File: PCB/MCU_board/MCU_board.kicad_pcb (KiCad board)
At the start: 2 copper layers, 70 x 70 mm, 45 parts, among them IC1 NEO-F10N-00B, IC2 TXB0104PWR, IC3 ESP32-S3-WROOM-1-N4R8, IC6 4259-63, IC8 MAX98357AETE+T, J13 Conn_01x15, J14 Conn_01x15, J2 Speaker, J4 FXP612 (u.FL) 2, J5 FXP612 (u.FL) 1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

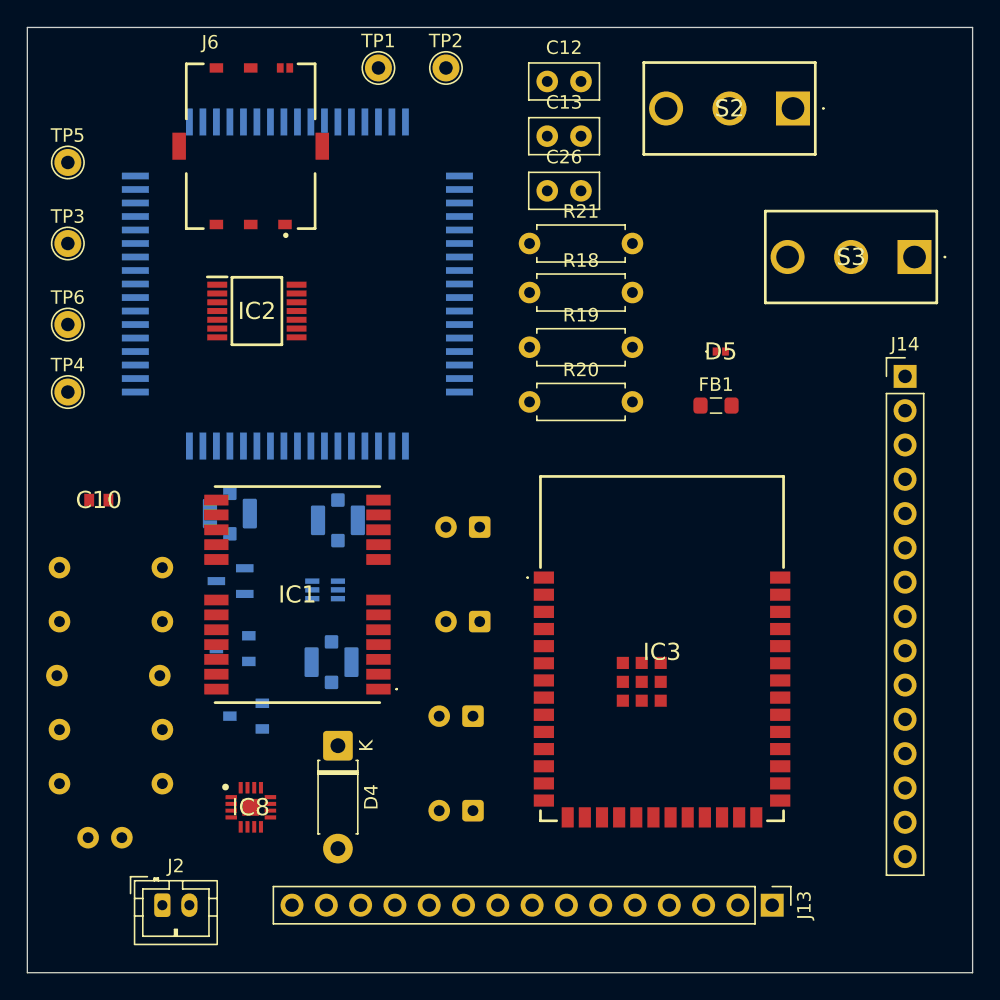
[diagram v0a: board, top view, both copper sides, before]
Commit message: routing and holes added
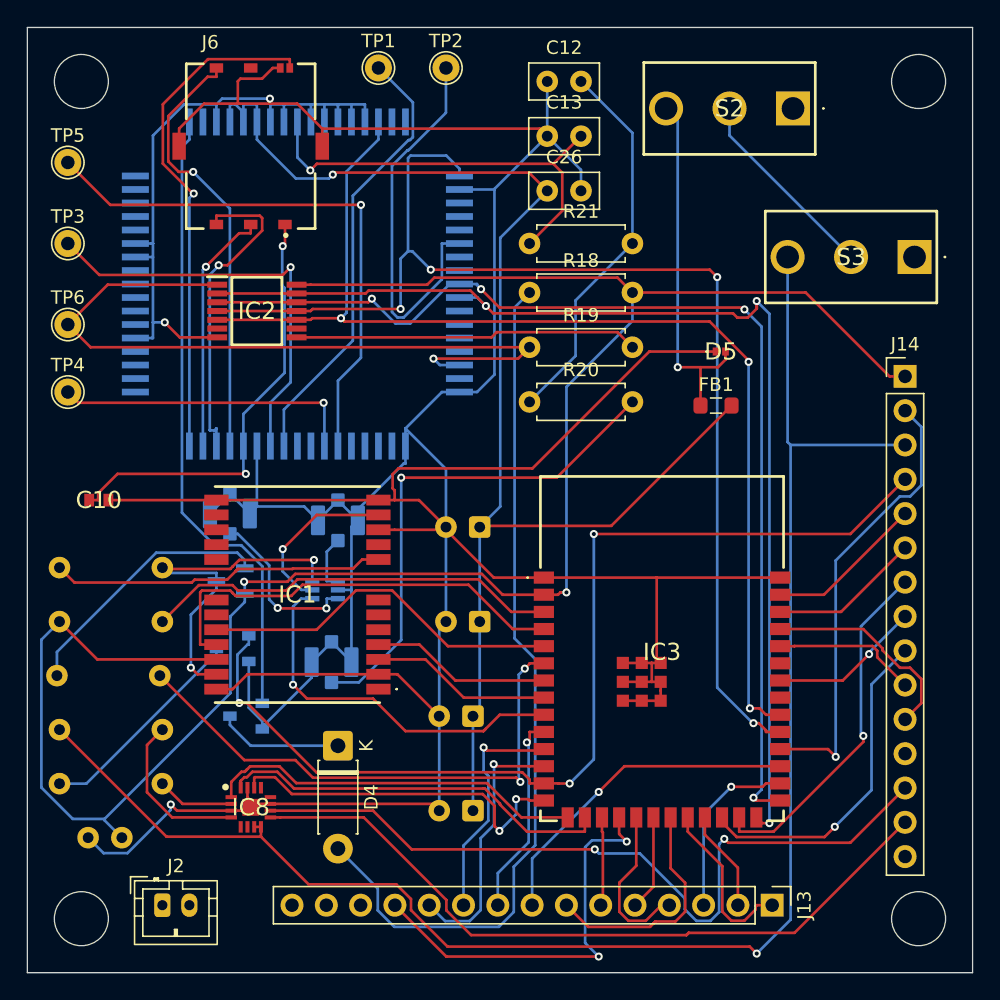
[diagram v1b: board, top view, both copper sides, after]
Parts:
- TP1: value TestPoint -> USB_DP
- TP2: value TestPoint -> BOOT_CFG
- TP3: value TestPoint -> USB_DM
- TP4: value TestPoint -> USB_VBUS
- TP5: value TestPoint -> MDM_LOG_TX
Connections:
- IC8 pad 10: Net-(IC8-OUTN) -> /OUT_N
- IC8 pad 9: Net-(IC8-OUTP) -> /OUT_P
- J14 pad 13: unconnected-(J14-Pin_13-Pad13) -> /OUT_N
- J14 pad 14: unconnected-(J14-Pin_14-Pad14) -> /OUT_P
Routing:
- net GND: track 0.00 -> 365.5 mm, vias 0 -> 3
- net /+3V3: track 0.00 -> 152.4 mm, vias 0 -> 2
- net /OUT+5V: track 0.00 -> 121.4 mm, vias 0 -> 1
- net Net-(U2-VBAT@1): track 0.00 -> 101.5 mm, vias 0 -> 1
- net /PWRKEY: track 0.00 -> 90.4 mm, vias 0 -> 4
- net /GSM_RXT: track 0.00 -> 86.4 mm, vias 0 -> 3
- net /STATUS: track 0.00 -> 85.0 mm, vias 0 -> 3
- net /GSM_TXD: track 0.00 -> 81.9 mm, vias 0 -> 4
- net /LOUDNESS: track 0.00 -> 76.5 mm, vias 0 -> 3
- net Net-(D4-A): track 0.00 -> 64.5 mm
- net /OUT_N: track 0.00 -> 58.1 mm, vias 0 -> 2
- net /Stationary/GSM_sheet/OUT1.8V: track 0.00 -> 56.8 mm, vias 0 -> 1
- net /OUT_P: track 0.00 -> 54.8 mm
- net Net-(Q5-G): track 0.00 -> 46.9 mm
- net Net-(U2-MDM_LOG_TX): track 0.00 -> 41.6 mm, vias 0 -> 1
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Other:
- outline, holes or cut-outs redrawn
- board text added: "Conn_01x15"

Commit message: everything before jlc template
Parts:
- removed J13, J14: Conn_01x15, Connector_PinHeader_2.54mm:PinHeader_1x15_P2.54mm_Vertical
- removed J2: Speaker, Connector_JST:JST_PH_B2B-PH-K_1x02_P2.00mm_Vertical
- added C1: 100nF, Capacitor_THT:C_Disc_D5.0mm_W2.5mm_P2.50mm, F.Cu at (219.5, 84.0)
- added C2: 1μF, Capacitor_THT:C_Disc_D5.0mm_W2.5mm_P2.50mm, F.Cu at (211.0, 94.0)
- added C3: 100nF, Capacitor_THT:C_Disc_D5.0mm_W2.5mm_P2.50mm, F.Cu at (211.0, 98.1)
- added J1: DS1013-40SSIB1-B-0, DS1013-40SSIB1-B-0:DS101340SSIB1B0, F.Cu at (236.0, 93.3)
- added R30: 10kΩ, Resistor_THT:R_Axial_DIN0207_L6.3mm_D2.5mm_P7.62mm_Horizontal, F.Cu at (255.0, 98.8)
- added S1: 1825910-6, 1825910-6:18259106, F.Cu at (219.5, 93.0)
- added S4: 1825910-6, 1825910-6:18259106, F.Cu at (242.5, 93.0)
- C22: value 100nF -> 1000nF
- moved R18 24.0 mm to (254.2, 42.6)
- moved R19 24.0 mm to (254.2, 46.7)
- moved R20 24.0 mm to (254.2, 50.7)
- moved R21 24.0 mm to (254.2, 39.0)
- moved D5 12.6 mm to (249.3, 42.0)
- moved FB1 12.6 mm to (249.0, 46.0)
- moved IC3 11.8 mm to (252.8, 75.3)
- moved C13 10.8 mm to (242.5, 42.0)
- moved C26 10.8 mm to (242.5, 46.0)
- moved S3 10.0 mm to (259.4, 57.0)
- moved IC8 3.62 mm to (207.8, 85.5)
- moved D4 3.01 mm to (214.0, 83.0)
- moved S2 2.02 mm to (250.4, 34.0)
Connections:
- IC3 pad 13: /LOUDNESS -> /USB_D-
- IC3 pad 14: /G_LRCLK -> /USB_D+
- IC3 pad 26: /GSM_RXT -> unconnected-(IC3-IO45-Pad26)
- IC3 pad 27: /GSM_TXD -> Net-(IC3-IO0)
- IC3 pad 33: unconnected-(IC3-IO40-Pad33) -> /GSM_RXT
- IC3 pad 34: /STAT2 -> /GSM_TXD
- IC3 pad 35: unconnected-(IC3-IO42-Pad35) -> /STAT2
- IC3 pad 38: /USB_D- -> /LOUDNESS
- IC3 pad 39: /USB_D+ -> /G_LRCLK
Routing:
- net /+3V3: track 152.4 -> 224.6 mm
- net GND: track 365.5 -> 437.6 mm, vias 3 -> 7
- net /G_LRCLK: track 26.4 -> 90.5 mm, vias 2 -> 6
- net /ACCEL_CS: track 12.6 -> 64.7 mm, vias 0 -> 1
- net /DATA_IN: track 7.07 -> 58.1 mm, vias 0 -> 3
- net Net-(IC3-EN): track 30.9 -> 77.1 mm, vias 0 -> 4
- net /STATUS: track 85.0 -> 130.3 mm, vias 3 -> 5
- net /STAT2: track 11.3 -> 48.9 mm, vias 1 -> 2
- net /ANTENA_SW: track 28.2 -> 64.1 mm
- net /ACCEL_INT1: track 7.51 -> 43.3 mm, vias 0 -> 2
- net /OUT+5V: track 121.4 -> 87.5 mm, vias 1 -> 0
- net /IMU_CS: track 6.59 -> 36.4 mm, vias 0 -> 1
- net Net-(IC3-IO0): track 0.00 -> 27.9 mm
- net /ACCEL_INT2: track 13.3 -> 40.2 mm, vias 1 -> 4
- net /Stationary/GSM_sheet/OUT1.8V: track 56.8 -> 83.3 mm, vias 1 -> 2
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
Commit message: routing on your own
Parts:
- removed C2: 1μF, Capacitor_THT:C_Disc_D5.0mm_W2.5mm_P2.50mm
- removed D5: PESD3V3L1BSLZ, PESD3V3L1BSLZ:PESD3V3L1BSLZ
- removed Q4: BSS138, BSS138:SOT95P240X120-3N
- removed S2, S3: SLW-1276864-4A-D, SLW-1276864-4A-D:SLW12768644AD
- added C4: 1μF, Capacitor_THT:CP_Radial_Tantal_D5.0mm_P2.50mm, F.Cu at (119.0, 120.5)
- added D1: PESD5V0C1BSFYL, PESD5V0C1BSFYL:PMEG3005AESFYL, B.Cu at (54.4, 128.0)
- C1: value 100nF -> 1μF
- C10, FB1, IC1, J6: moved to B.Cu
- C22: footprint Capacitor_THT:CP_Radial_Tantal_D5.0mm_P2.50mm -> Capacitor_THT:C_Disc_D5.0mm_W2.5mm_P2.50mm; moved to F.Cu
- C23: value 100µF -> 1000µF; moved to F.Cu
- C24, C25, C8, IC6, J4, J5, J7, Q3, R17, R26, R29, U2: moved to F.Cu
- R16: value 680kΩ -> 100kΩ; moved to F.Cu
- moved R18 237.3 mm to (40.8, 146.5), turned to 180 degrees
- moved R21 228.9 mm to (49.5, 141.5), turned to -90 degrees
- moved R20 224.0 mm to (58.5, 159.7), turned to -90 degrees
- moved C13 214.7 mm to (49.0, 135.0), turned to -90 degrees
- moved FB1 212.5 mm to (52.0, 125.7), turned to -90 degrees
- moved TP1 209.3 mm to (32.9, 126.8), turned to 180 degrees
- moved C12 209.2 mm to (61.4, 154.3), turned to 180 degrees
- moved C26 203.3 mm to (62.0, 139.5), turned to -90 degrees
- moved C25 199.8 mm to (34.2, 140.5)
- moved C24 198.2 mm to (37.8, 140.0), turned to 0 degrees
- moved R19 197.1 mm to (90.2, 156.0)
- moved R28 192.1 mm to (35.5, 162.3), turned to 90 degrees
- moved J6 190.7 mm to (37.0, 117.9), turned to -90 degrees
- moved IC1 188.8 mm to (47.0, 160.0), turned to 180 degrees
- moved C22 186.2 mm to (54.0, 134.5), turned to 0 degrees
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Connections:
- C8 pad 1: /+3V3 -> Net-(IC1-VCC)
- FB1 pad 1: Net-(D5-K2) -> /3V8
- IC1 pad 22: /+3V3 -> Net-(IC1-VCC)
- J1 pad 26: unconnected-(J1-Pad26) -> /3V8
- R16 pad 2: /OUT+5V -> /LOUDNESS
- R26 pad 2: Net-(Q4-D) -> GND
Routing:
- net GND: track 437.6 -> 0.00 mm, vias 7 -> 0
- net /+3V3: track 224.6 -> 0.00 mm, vias 2 -> 0
- net /STATUS: track 130.3 -> 0.00 mm, vias 5 -> 0
- net /PWRKEY: track 104.2 -> 0.00 mm, vias 4 -> 0
- net /G_LRCLK: track 90.5 -> 0.00 mm, vias 6 -> 0
- net /OUT+5V: track 87.5 -> 0.00 mm
- net /GSM_RXT: track 98.1 -> 11.6 mm, vias 3 -> 1
- net /GSM_TXD: track 85.2 -> 0.00 mm, vias 4 -> 0
- net Net-(D4-A): track 85.1 -> 4.48 mm, vias 1 -> 0
- net /Stationary/GSM_sheet/OUT1.8V: track 83.3 -> 11.9 mm, vias 2 -> 0
- net Net-(U2-VBAT@1): track 105.8 -> 35.0 mm
- net /ACCEL_CS: track 64.7 -> 0.00 mm, vias 1 -> 0
- net Net-(IC3-EN): track 77.1 -> 12.6 mm, vias 4 -> 0
- net Net-(J7-In): track 64.1 -> 0.00 mm, vias 1 -> 0
- net /OUT_P: track 59.5 -> 0.00 mm, vias 2 -> 0
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- added copper zone on In1.Cu, net /+3V3
- added copper zone on In2.Cu, net GND
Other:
- copper layers 2 -> 4

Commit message: routing done
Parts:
- moved C4 40.0 mm to (79.0, 120.3)
- moved C3 27.3 mm to (87.7, 120.5), turned to 180 degrees
- moved D1 20.3 mm to (46.1, 109.4)
- moved R30 16.0 mm to (78.2, 166.5), turned to 180 degrees
- moved FB1 13.5 mm to (54.6, 112.5), turned to 0 degrees
- moved C10 11.6 mm to (46.8, 116.3)
- moved C8 5.20 mm to (95.8, 118.8)
- moved Q3 3.91 mm to (97.3, 123.9)
- moved Q5 2.47 mm to (48.5, 123.8)
- moved J7 0.78 mm to (52.2, 156.3)
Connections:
- J1 pad 11: /USB_D- -> unconnected-(J1-Pad11)
- J1 pad 2: /WCLK -> /3V8
- J1 pad 20: /ACCEL_INT2 -> /ACCEL_INT1
- J1 pad 22: /ACCEL_INT1 -> /ACCEL_INT2
- J1 pad 26: /3V8 -> /WCLK
- J1 pad 37: unconnected-(J1-Pad37) -> /USB_D+
- J1 pad 39: unconnected-(J1-Pad39) -> /USB_D-
- J1 pad 6: /MOSI -> /MISO
- J1 pad 8: /MISO -> /MOSI
- J1 pad 9: /USB_D+ -> unconnected-(J1-Pad9)
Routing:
- net /+3V3: track 0.00 -> 179.2 mm, vias 0 -> 2
- net GND: track 0.00 -> 142.0 mm, vias 0 -> 36
- net /Stationary/GSM_sheet/OUT1.8V: track 11.9 -> 123.8 mm, vias 0 -> 2
- net /PWRKEY: track 0.00 -> 99.1 mm, vias 0 -> 5
- net /GSM_TXD: track 0.00 -> 98.2 mm, vias 0 -> 10
- net /STATUS: track 0.00 -> 92.6 mm, vias 0 -> 3
- net /GSM_RXT: track 11.6 -> 97.4 mm, vias 1 -> 7
- net Net-(IC1-VCC): track 49.6 -> 133.3 mm, vias 1 -> 4
- net /GSM_INT: track 0.00 -> 77.4 mm, vias 0 -> 6
- net /TXD: track 0.00 -> 76.4 mm, vias 0 -> 2
- net /RXD: track 0.00 -> 74.9 mm, vias 0 -> 2
- net /TIMEPULSE: track 0.00 -> 73.9 mm, vias 0 -> 6
- net /G_LRCLK: track 0.00 -> 54.8 mm, vias 0 -> 2
- net /OUT+5V: track 0.00 -> 51.7 mm, vias 0 -> 3
- net /TS/CTRL: track 0.00 -> 51.0 mm, vias 0 -> 2
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- added copper zone on In1.Cu, net GND
- removed copper zone on In1.Cu, net /+3V3
- removed copper zone on In2.Cu, net GND

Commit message: DRC passed
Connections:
- IC2 pad 2: /GSM_RXT -> /Stationary/GSM_sheet/GSM_RXD_1V8
- IC2 pad 3: /GSM_TXD -> /Stationary/GSM_sheet/GSM_TXD_1V8
- IC2 pad 4: /PWRKEY -> /Stationary/GSM_sheet/PWRKEY_1V8
- IC2 pad 5: /STATUS -> /Stationary/GSM_sheet/STATUS_1V8
- U2 pad P$1: /PWRKEY -> /Stationary/GSM_sheet/PWRKEY_1V8
- U2 pad P$10: /GSM_RXT -> /Stationary/GSM_sheet/GSM_RXD_1V8
- U2 pad P$66: /STATUS -> /Stationary/GSM_sheet/STATUS_1V8
- U2 pad P$9: /GSM_TXD -> /Stationary/GSM_sheet/GSM_TXD_1V8
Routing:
- net /GSM_TXD: track 98.2 -> 14.2 mm, vias 10 -> 2
- net /Stationary/GSM_sheet/GSM_TXD_1V8: track 0.00 -> 83.9 mm, vias 0 -> 6
- net /Stationary/GSM_sheet/GSM_RXD_1V8: track 0.00 -> 79.3 mm, vias 0 -> 5
- net /GSM_RXT: track 97.4 -> 18.1 mm, vias 7 -> 2
- net /Stationary/GSM_sheet/PWRKEY_1V8: track 0.00 -> 72.6 mm, vias 0 -> 3
- net /PWRKEY: track 99.1 -> 26.5 mm, vias 5 -> 2
- net /STATUS: track 92.6 -> 28.9 mm, vias 3 -> 2
- net /Stationary/GSM_sheet/STATUS_1V8: track 0.00 -> 62.8 mm, vias 0 -> 2

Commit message: everything checked
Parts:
- added C2: 100nF, Capacitor_THT:C_Disc_D5.0mm_W2.5mm_P2.50mm, F.Cu at (49.0, 138.4)
- added H1: MountingHole, MountingHole:MountingHole_3.2mm_M3_Pad_Via, F.Cu at (33.6, 103.5)
- added H2: MountingHole, MountingHole:MountingHole_3.2mm_M3_Pad_Via, F.Cu at (96.5, 103.5)
- added H3: MountingHole, MountingHole:MountingHole_3.2mm_M3_Pad_Via, F.Cu at (33.5, 166.5)
- added H4: MountingHole, MountingHole:MountingHole_3.2mm_M3_Pad_Via, F.Cu at (96.5, 166.5)
- IC1: moved to F.Cu
- moved R20 64.4 mm to (86.3, 101.6)
- moved J7 58.5 mm to (80.5, 105.0)
- moved C12 53.6 mm to (72.8, 101.9), turned to 0 degrees
- moved R21 52.7 mm to (91.2, 109.3), turned to 90 degrees
- moved C13 37.2 mm to (65.8, 101.8), turned to 0 degrees
- moved S1 5.41 mm to (84.8, 120.1)
- moved C1 3.98 mm to (93.2, 114.8)
- moved R28 3.91 mm to (34.2, 158.6)
- moved C3 3.35 mm to (89.2, 123.5)
- moved R17 1.40 mm to (92.7, 125.0)
- moved R29 0.82 mm to (97.2, 115.9)
- turned IC1 to 0 degrees
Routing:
- net /Stationary/GSM_sheet/SIM_POWER: track 14.1 -> 37.0 mm
- net Net-(IC1-RESET_N): track 6.62 -> 27.7 mm, vias 0 -> 1
- net /TXD: track 76.4 -> 88.4 mm, vias 2 -> 3
- net /RXD: track 74.9 -> 86.9 mm, vias 2 -> 3
- net Net-(U2-RF_ANT): track 39.6 -> 47.2 mm, vias 1 -> 0
- net /GSM_INT: track 77.4 -> 70.5 mm
- net GND: track 142.0 -> 135.6 mm
- net Net-(J7-In): track 12.7 -> 7.02 mm, vias 1 -> 0
- net Net-(IC1-RF_IN): track 68.2 -> 63.3 mm, vias 1 -> 0
- net /TIMEPULSE: track 73.9 -> 76.2 mm
- net /+3V3: track 179.2 -> 181.3 mm, vias 2 -> 4
- net /Stationary/GSM_sheet/PWRKEY_1V8: track 72.6 -> 71.1 mm, vias 3 -> 4
- net Net-(Q3-G): track 8.50 -> 7.31 mm
- net /GSM_POWER: track 4.22 -> 3.04 mm
- net Net-(C12-Pad2): track 17.0 -> 16.0 mm
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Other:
- board size 70 x 70 mm -> 73 x 73 mm

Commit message: everything done before changing footprints
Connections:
- J1 pad 40: unconnected-(J1-Pad40) -> GND
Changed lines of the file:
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@@
 			(disableapertmacros no)
 			(usegerberextensions no)
-			(usegerberattributes yes)
-			(usegerberadvancedattributes yes)
+			(usegerberattributes no)
+			(usegerberadvancedattributes no)
 			(creategerberjobfile yes)
 			(dashed_line_dash_ratio 12)
@@
 			(outputformat 1)
 			(mirror no)
-			(drillshape 1)
+			(drillshape 0)
 			(scaleselection 1)
-			(outputdirectory "")
+			(outputdirectory "gerbers_mcu/")
 		)
 	)
@@
 			(layers "*.Cu" "*.Mask")
 			(remove_unused_layers no)
-			(net "unconnected-(J1-Pad40)")
+			(net "GND")
 			(pinfunction "40_40")
-			(pintype "passive+no_connect")
+			(pintype "passive")
 		)
 		(embedded_fonts no)
@@
 		(tags "Capacitor")
 		(property "Reference" "C10"
-			(at 0 0 90)
+			(at 0 1.65 90)
 			(layer "B.SilkS")
 			(effects
@@
 		)
 		(fp_text user "${REFERENCE}"
-			(at 0 0 90)
+			(at 0.46 1.65 90)
 			(layer "B.Fab")
 			(effects
@@
 		)
 		(property "Value" "SIM8055-6-1-14-00-A"
-			(at 6.99918 -9.8626 90)
+			(at -1.8 -11.69 90)
 			(layer "B.Fab")
 			(effects
@@
 			)
 		)
+	)
+	(dimension
+		(type orthogonal)
+		(layer "F.Cu")
+		(pts
+			(xy 96.45 100.25) (xy 96.45 106.65)
+		)
+		(height 14.55)
+		(orientation 1)
+		(format
+			(prefix "")
+			(suffix "")
+			(units 3)
+			(units_format 0)
+			(precision 4)
+			(suppress_zeroes yes)
+		)
+		(style
+			(thickness 0.2)
+			(arrow_length 1.27)
+			(text_position_mode 0)
+			(arrow_direction outward)
+			(extension_height 0.58642)
+			(extension_offset 0.5)
+			(keep_text_aligned yes)
+		)
+		(gr_text "6.4"
+			(at 109.2 103.45 90)
+			(layer "F.Cu")
+			(effects
+				(font
+					(size 1.5 1.5)
+					(thickness 0.3)
+				)
+			)
+		)
+	)
+	(dimension
+		(type orthogonal)
+		(layer "F.Cu")
+		(pts
+			(xy 99.75 166.5) (xy 101.5 166.5)
+		)
+		(height 8.3)
+		(orientation 0)
+		(format
+			(prefix "")
+			(suffix "")
+			(units 3)
+			(units_format 0)
+			(precision 4)
+			(suppress_zeroes yes)
+		)
+		(style
+			(thickness 0.2)
+			(arrow_length 1.27)
+			(text_position_mode 0)
+			(arrow_direction outward)
+			(extension_height 0.58642)
+			(extension_offset 0.5)
+			(keep_text_aligned yes)
+		)
+		(gr_text "1.75"
+			(at 100.625 173 0)
+			(layer "F.Cu")
+			(effects
+				(font
+					(size 1.5 1.5)
+					(thickness 0.3)
+				)
+			)
+		)
+	)
+	(dimension
+		(type orthogonal)
+		(layer "F.Cu")
+		(pts
+			(xy 96.45 100.25) (xy 96.45 98.45)
+		)
+		(height 12.65)
+		(orientation 1)
+		(format
+			(prefix "")
+			(suffix "")
+			(units 3)
+			(units_format 0)
+			(precision 4)
+			(suppress_zeroes yes)
+		)
+		(style
+			(thickness 0.2)
+			(arrow_length 1.27)
+			(text_position_mode 0)
+			(arrow_direction outward)
+			(extension_height 0.58642)
+			(extension_offset 0.5)
+			(keep_text_aligned yes)
+		)
+		(gr_text "1.8"
+			(at 107.3 99.35 90)
+			(layer "F.Cu")
+			(effects
+				(font
+					(size 1.5 1.5)
+					(thickness 0.3)
+				)
+			)
+		)
+	)
+	(dimension
+		(type orthogonal)
+		(layer "F.Cu")
+		(pts
+			(xy 99.65 103.45) (xy 101.4 103.45)
+		)
+		(height -6.85)
+		(orientation 0)
+		(format
+			(prefix "")
+			(suffix "")
+			(units 3)
+			(units_format 0)
+			(precision 4)
+			(suppress_zeroes yes)
+		)
+		(style
+			(thickness 0.2)
+			(arrow_length 1.27)
+			(text_position_mode 0)
+			(arrow_direction outward)
+			(extension_height 0.58642)
+			(extension_offset 0.5)
+			(keep_text_aligned yes)
+		)
+		(gr_text "1.75"
+			(at 100.525 94.8 0)
+			(layer "F.Cu")
+			(effects
+				(font
+					(size 1.5 1.5)
+					(thickness 0.3)
+				)
+			)
+		)
+	)
+	(dimension
+		(type orthogonal)
+		(layer "F.Cu")
+		(pts
+			(xy 96.55 166.5) (xy 99.65 103.45)
+		)
+		(height 8.75)
+		(orientation 1)
+		(format
+			(prefix "")
+			(suffix "")
+			(units 3)
+			(units_format 0)
+			(precision 4)
+			(suppress_zeroes yes)
+		)
+		(style
+			(thickness 0.2)
+			(arrow_length 1.27)
+			(text_position_mode 0)
+			(arrow_direction outward)
+			(extension_height 0.58642)
+			(extension_offset 0.5)
+			(keep_text_aligned yes)
+		)
+		(gr_text "63.05"
+			(at 103.5 134.975 90)
+			(layer "F.Cu")
+			(effects
+				(font
+					(size 1.5 1.5)
+					(thickness 0.3)
+				)
+			)
+		)
+	)
+	(dimension
+		(type orthogonal)
+		(layer "F.Cu")
+		(pts
+			(xy 96.55 169.7) (xy 96.55 171.5)
+		)
+		(height 13.45)
+		(orientation 1)
+		(format
+			(prefix "")
+			(suffix "")
+			(units 3)
+			(units_format 0)
+			(precision 4)
+			(suppress_zeroes yes)
+		)
+		(style
+			(thickness 0.2)
+			(arrow_length 1.27)
+			(text_position_mode 0)
+			(arrow_direction outward)
+			(extension_height 0.58642)
+			(extension_offset 0.5)
+			(keep_text_aligned yes)
+		)
+		(gr_text "1.8"
+			(at 108.2 170.6 90)
+			(layer "F.Cu")
+			(effects
+				(font
+					(size 1.5 1.5)
+					(thickness 0.3)
+				)
+			)
+		)
